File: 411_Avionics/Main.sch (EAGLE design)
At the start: 17 parts, among them IC1 BQ24022, U1 USB_In, U3 LSM9DS0

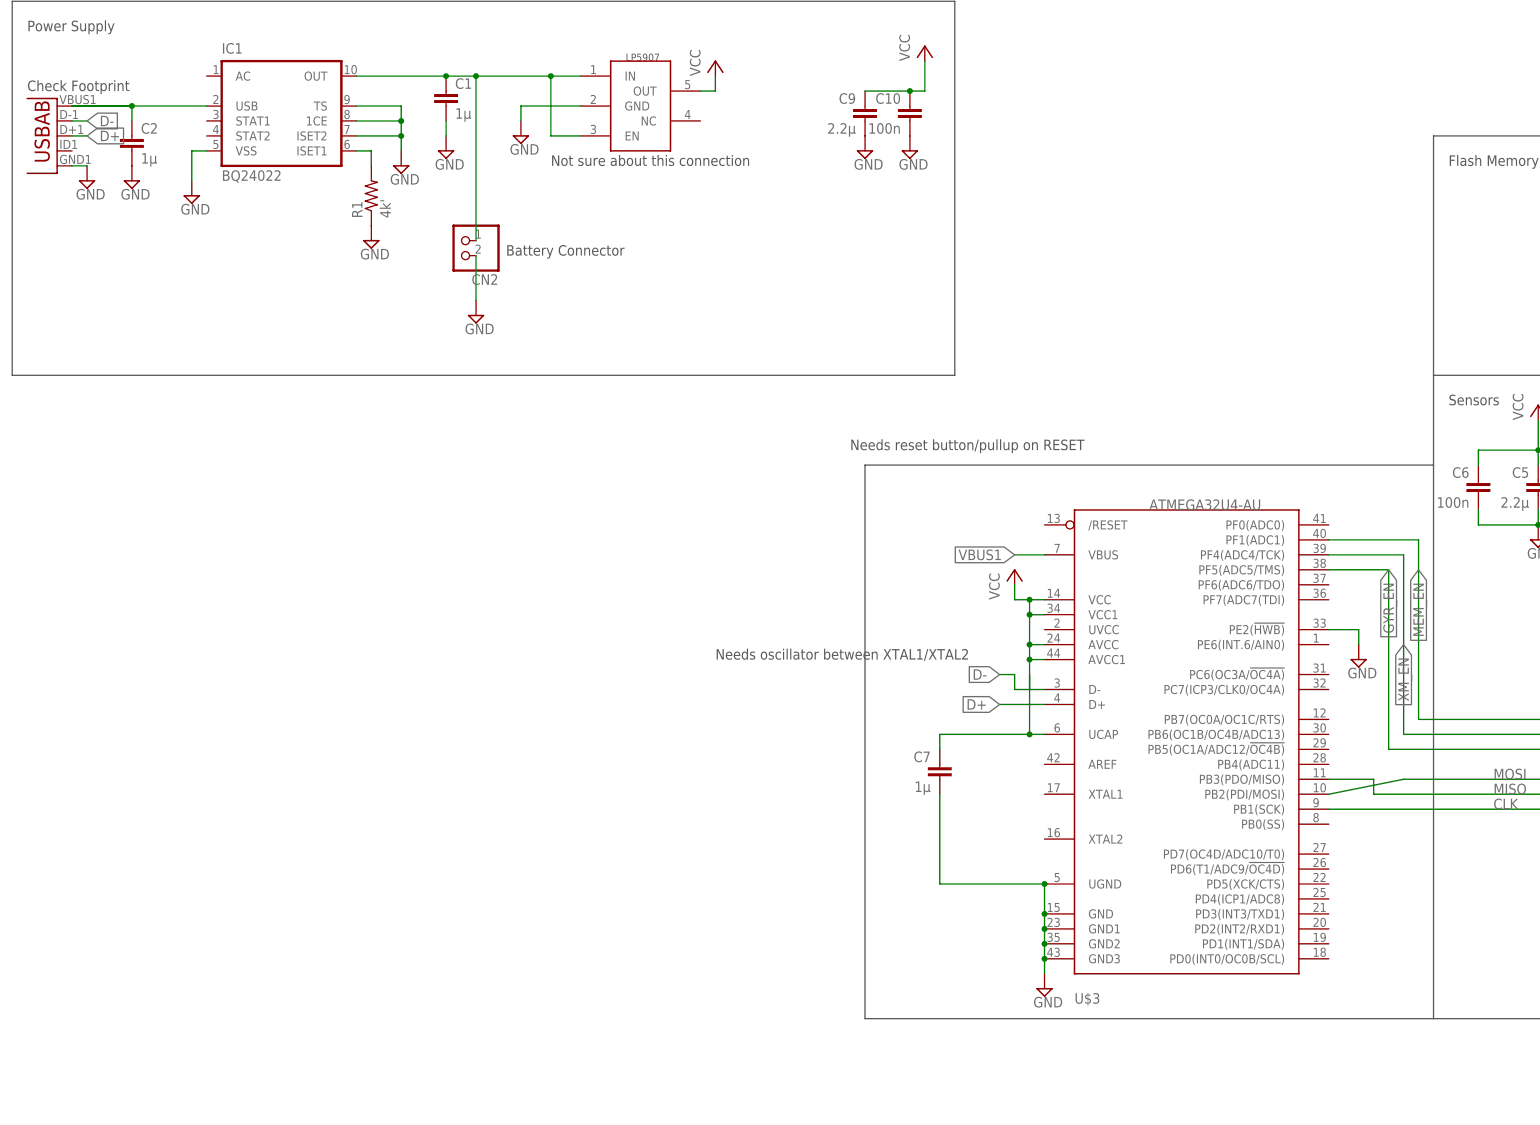
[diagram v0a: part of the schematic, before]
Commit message: Added RESET switch and Oscillator to schematic
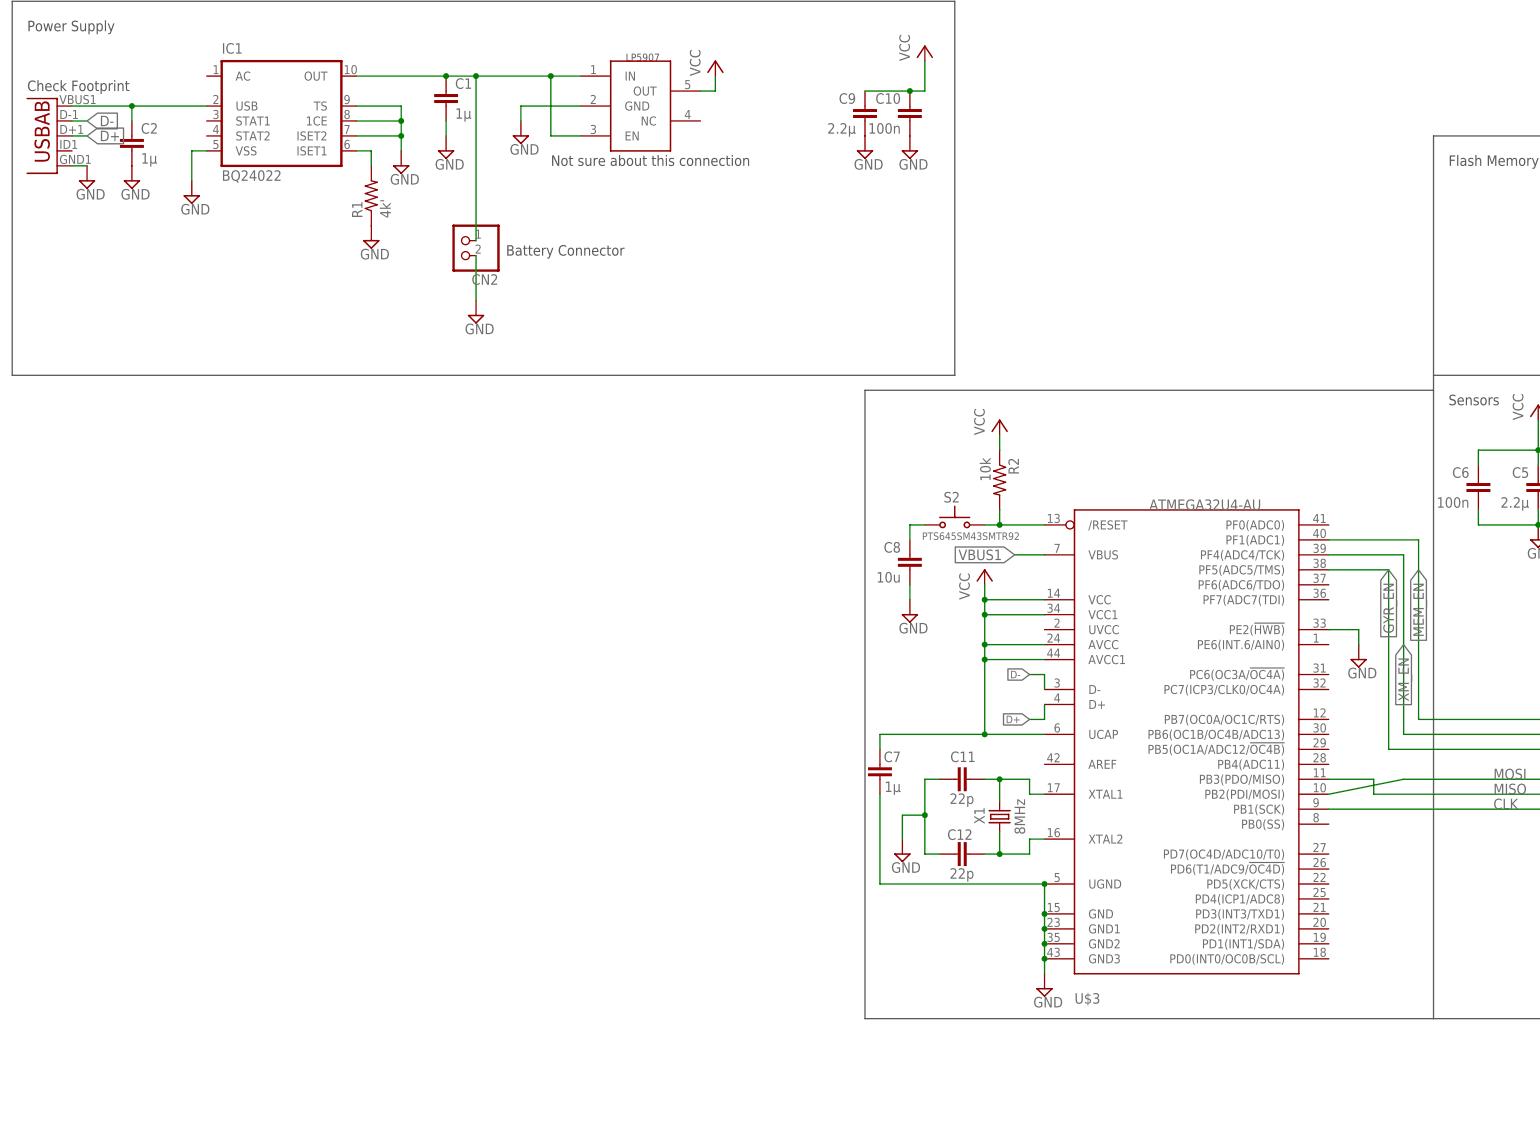
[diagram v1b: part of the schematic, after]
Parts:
- added C11, C12: 22p, rcl:C-EUC0805
- added C8: 10u, rcl:C-EUC0805
- added R2: 10k, rcl:R-US_0309/12
- added S2: PTS645SM43SMTR92, switch-ck:PTS645SSMTR
- added X1: 8MHz, IQD-Frequency-Products:CRYSTALS-NOGND-HC49/4H
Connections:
- new net N$2: C11.1, U$3.XTAL1, X1.1
- new net N$3: R2.2, S2.S, U$3./RESET
- new net N$5: C12.1, U$3.XTAL2, X1.2
- new net N$6: C8.1, S2.P
- net GND: now also C11.2, C12.2, C8.2
- net VCC: now also R2.1
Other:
- note removed: "Needs oscillator between XTAL1/XTAL2"
- note removed: "Needs reset button/pullup on RESET"
- moved on the sheet: C7
